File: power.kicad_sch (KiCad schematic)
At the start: 78 parts, among them J3 Vcore_sel, U1 TLV62569DBV, U3 MPM3833CGRH-Z, U4 GateMate-CCGM1A1, U5 TLV62569DBV

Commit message: Initial version of 0.2
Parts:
- R105, R106, R23: value 1R -> 4R7
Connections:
- net VDD_CORE: now also C127.1, C128.1, C42.1; no longer C120.1, C121.1, C122.1, C123.1, C124.1, C125.1, C33.1, C36.1, C39.1
- net VDD_PLL: now also C33.1, C36.1, C39.1; no longer C42.1
- net VDD_SER: now also C121.1, C123.1, C125.1; no longer C128.1
- net VDD_SER_PLL: now also C120.1, C122.1, C124.1; no longer C127.1
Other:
- note removed: "Needs to be 3.3V input"
- moved on the sheet: C120, C121, C122, C123, C124, C125, C127, C128, C2, C33, C36, C39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

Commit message: Update stackup
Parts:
- R105, R106, R23: value 4R7 -> 2R
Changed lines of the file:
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@@
 			)
 		)
-		(property "Value" "4R7"
+		(property "Value" "2R"
 			(at 151.13 114.3 90)
 			(show_name no)
@@
 			)
 		)
-		(property "Value" "4R7"
+		(property "Value" "2R"
 			(at 152.4 88.9 90)
 			(show_name no)
@@
 			)
 		)
-		(property "Value" "4R7"
+		(property "Value" "2R"
 			(at 152.4 140.462 90)
 			(show_name no)

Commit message: M2 key update - changing resistors back to 1R
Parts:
- R105, R106, R23: value 2R -> 1R; LCSC (none) -> C22936
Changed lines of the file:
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@@
 			)
 		)
-		(property "Value" "2R"
+		(property "Value" "1R"
 			(at 151.13 114.3 90)
 			(show_name no)
@@
 			)
 		)
-		(property "LCSC" ""
+		(property "LCSC" "C22936"
 			(at 151.13 111.76 0)
 			(hide yes)
@@
 			)
 		)
-		(property "Value" "2R"
+		(property "Value" "1R"
 			(at 152.4 88.9 90)
 			(show_name no)
@@
 			)
 		)
-		(property "LCSC" ""
+		(property "LCSC" "C22936"
 			(at 152.4 86.36 0)
 			(hide yes)
@@
 			)
 		)
-		(property "Value" "2R"
+		(property "Value" "1R"
 			(at 152.4 140.462 90)
 			(show_name no)
@@
 			)
 		)
-		(property "LCSC" ""
+		(property "LCSC" "C22936"
 			(at 152.4 138.43 0)
 			(hide yes)

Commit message: initial version of ULX5-PCIe-1x
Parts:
- J3: footprint Jumper:SolderJumper-3_P1.3mm_Open_RoundedPad1.0x1.5mm -> Jumper:SolderJumper-3_P1.3mm_Bridged2Bar12_RoundedPad1.0x1.5mm
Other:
- note added: "Not used - for now - colud be used for MIPI?"

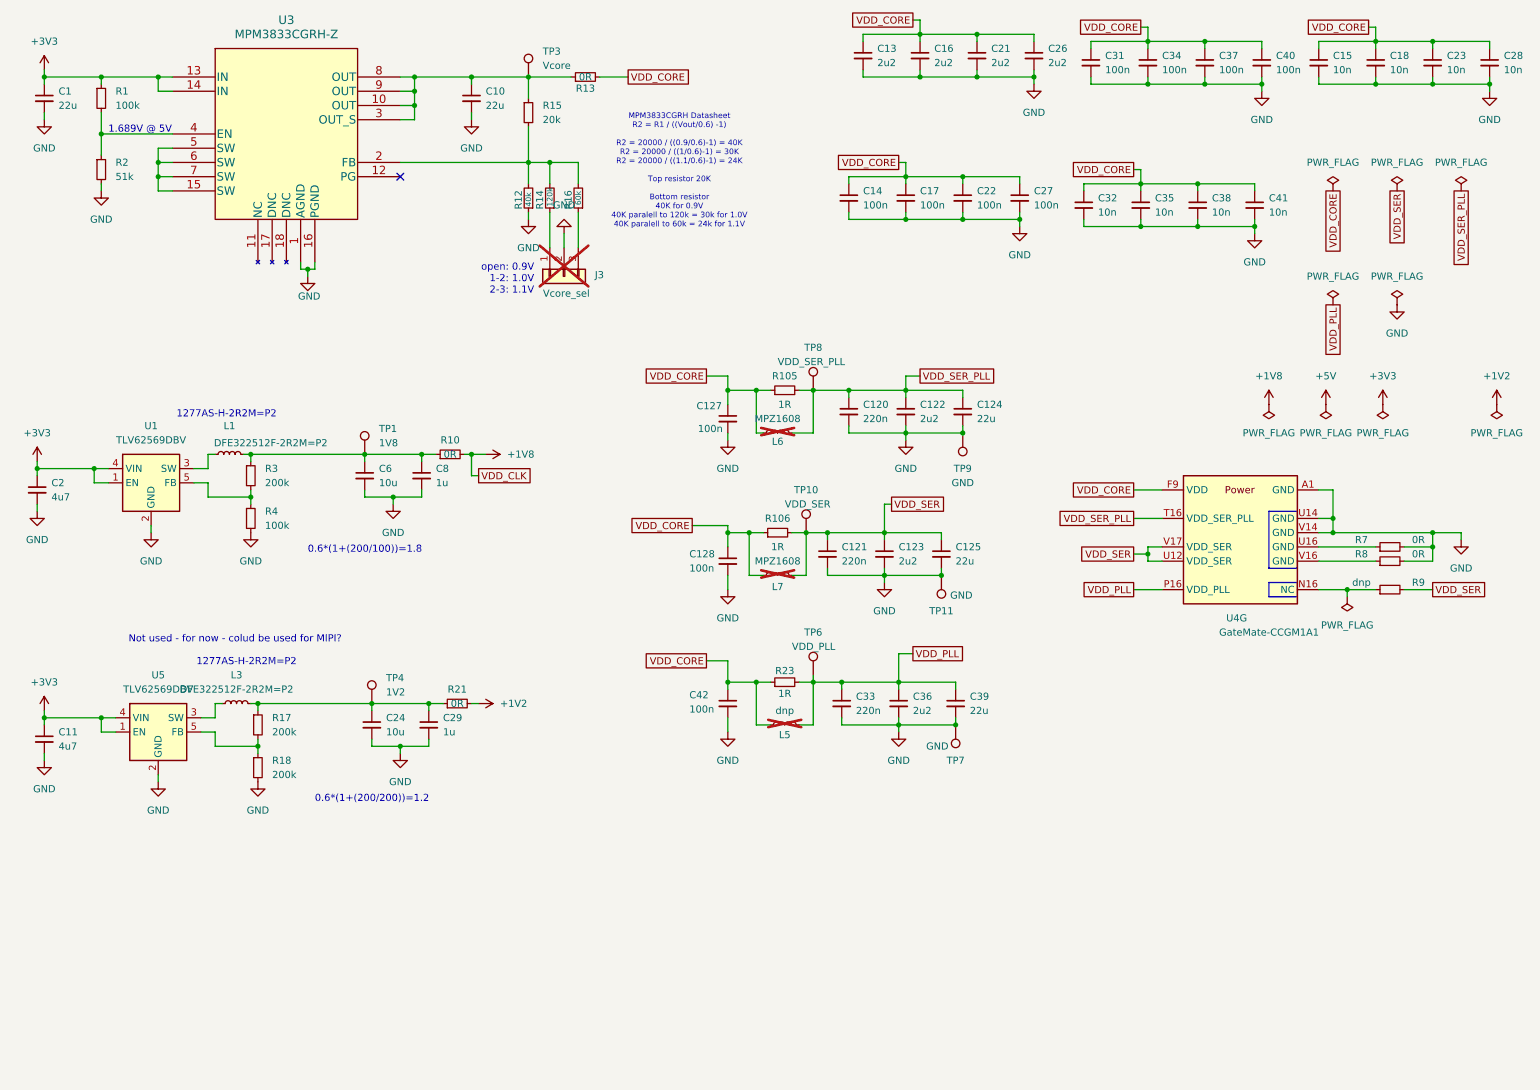
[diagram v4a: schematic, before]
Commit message: Adding 12V PSU
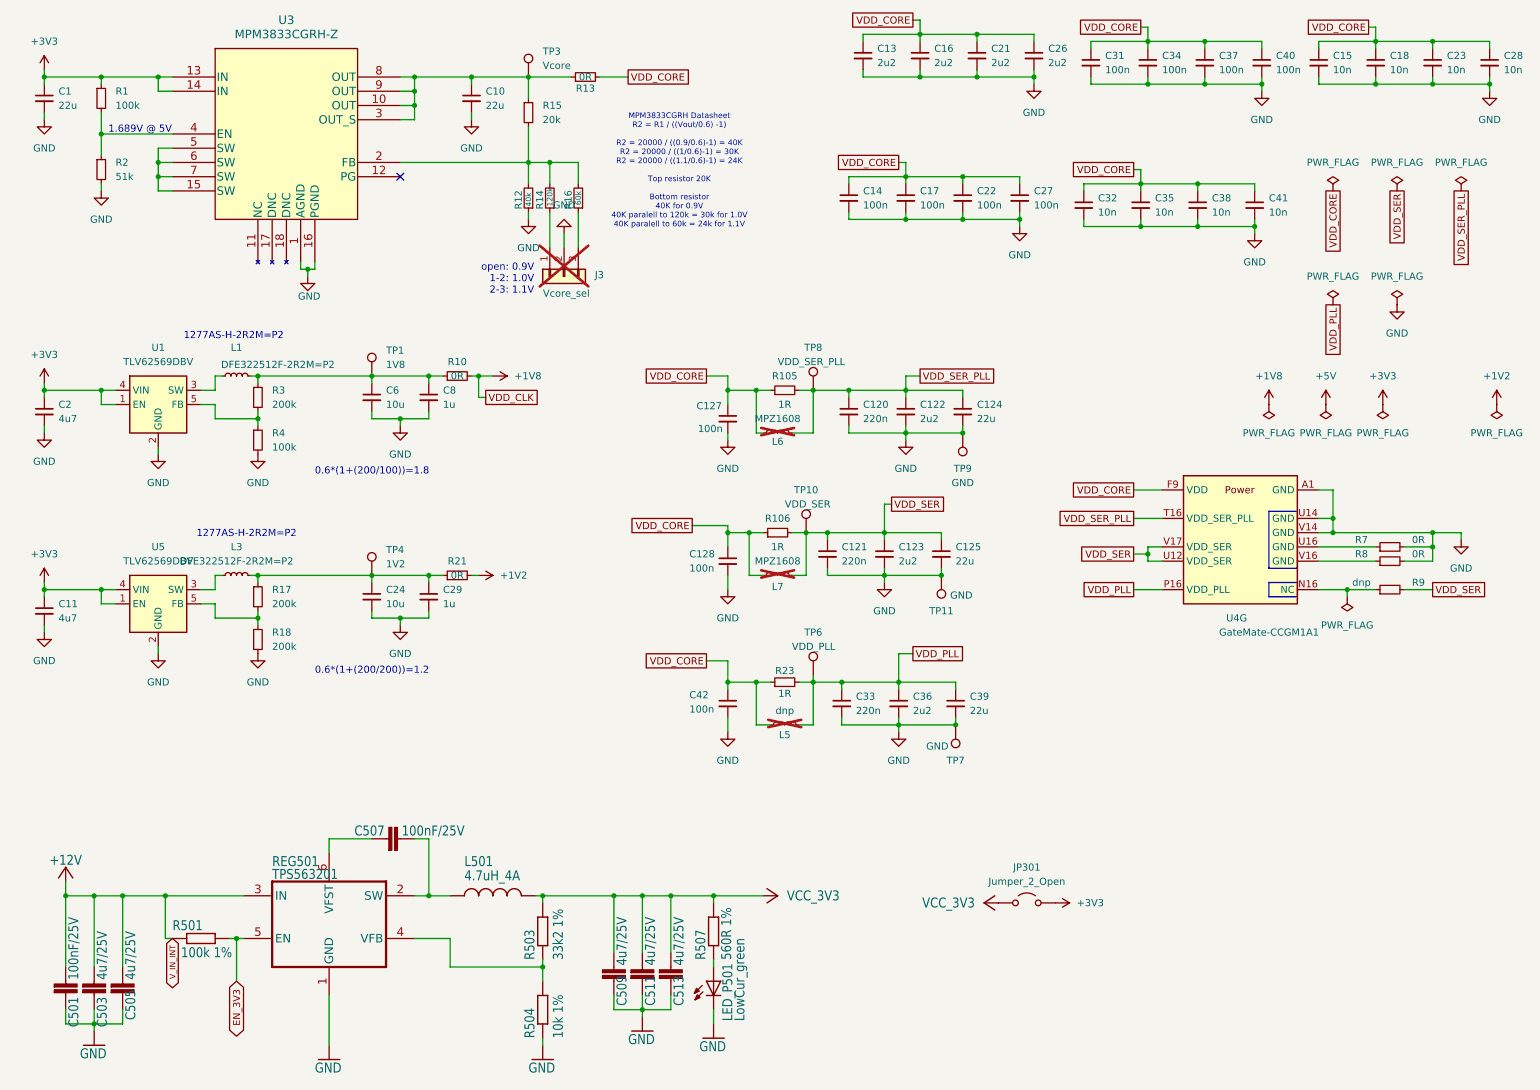
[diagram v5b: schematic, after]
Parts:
- added C501, C507: 100nF/25V, Capacitor_SMD:C_0402_1005Metric, symbol M-SU-12V-v1r1-eagle-import:C0402
- added C503, C505, C509, C511, C513: 4u7/25V, Capacitor_SMD:C_0402_1005Metric, symbol M-SU-12V-v1r1-eagle-import:C0402
- added JP301: Jumper_2_Open, Jumper:SolderJumper-2_P1.3mm_Open_RoundedPad1.0x1.5mm, symbol Jumper:Jumper_2_Open
- added L501: 4.7uH_4A, M-SU-12V-v1r1-import-fps:YSPI0530, symbol M-SU-12V-v1r1-eagle-import:YSPI0530
- added LED_P501: LowCur_green, LED_SMD:LED_0603_1608Metric, symbol M-SU-12V-v1r1-eagle-import:LED0603
- added R501: 100k 1%, Resistor_SMD:R_0402_1005Metric, symbol M-SU-12V-v1r1-eagle-import:R0402
- added R503: 33k2 1%, Resistor_SMD:R_0402_1005Metric, symbol M-SU-12V-v1r1-eagle-import:R0402
- added R504: 10k 1%, Resistor_SMD:R_0402_1005Metric, symbol M-SU-12V-v1r1-eagle-import:R0402
- added R507: 560R 1%, Resistor_SMD:R_0402_1005Metric, symbol M-SU-12V-v1r1-eagle-import:R0402
- added REG501: TPS563201, M-SU-12V-v1r1-import-fps:SOT-23-THIN, symbol M-SU-12V-v1r1-eagle-import:TPS563201
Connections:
- net +3V3: now also JP301.2 (B)
- net GND: now also C501.2, C503.2, C505.2, C509.2, C511.2, C513.2, LED_P501.C, R504.1, REG501.1 (GND)
- new net: C507.1, L501.1, REG501.2 (SW)
- new net: C507.2, REG501.6 (VFST)
- new net: R503.1, R504.2, REG501.4 (VFB)
- new net: LED_P501.A, R507.1
- new net +12V: C501.1, C503.1, C505.1, R501.1, REG501.3 (IN)
- new net EN_3V3: R501.2, REG501.5 (EN)
- new net VCC_3V3: C509.1, C511.1, C513.1, JP301.1 (A), L501.2, R503.2, R507.2
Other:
- note removed: "Not used - for now - colud be used for MIPI?"
- moved on the sheet: C11, C2, C24, C29, C6, C8, L1, L3, R10, R17, R18, R21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

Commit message: Pair switch
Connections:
- net GND: now also LED_P501.1; no longer LED_P501.C
- net at R507.1: now also LED_P501.2; no longer LED_P501.A
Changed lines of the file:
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@@
 			)
 		)
-		(pin "C"
+		(property "LCSC" ""
+			(at 139.7 191.77 0)
+			(hide yes)
+			(show_name no)
+			(do_not_autoplace no)
+			(effects
+				(font
+					(size 1.27 1.27)
+				)
+			)
 		)
-		(pin "A"
+		(pin "2"
+		)
+		(pin "1"
 		)
 		(instances

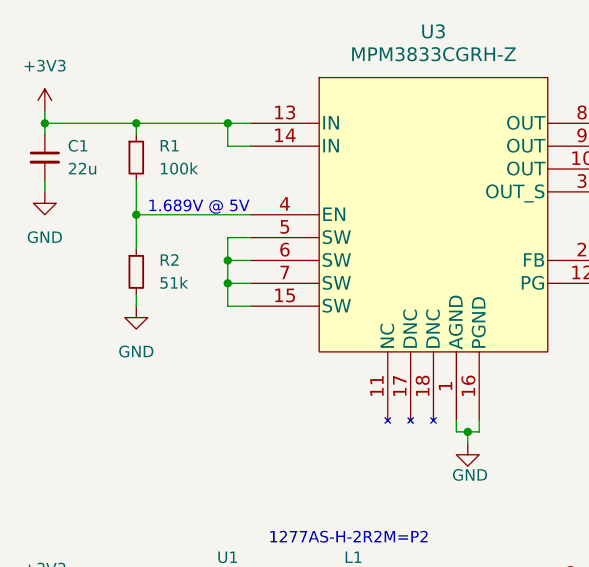
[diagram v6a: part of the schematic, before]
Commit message: power enable fix - connecting AGND
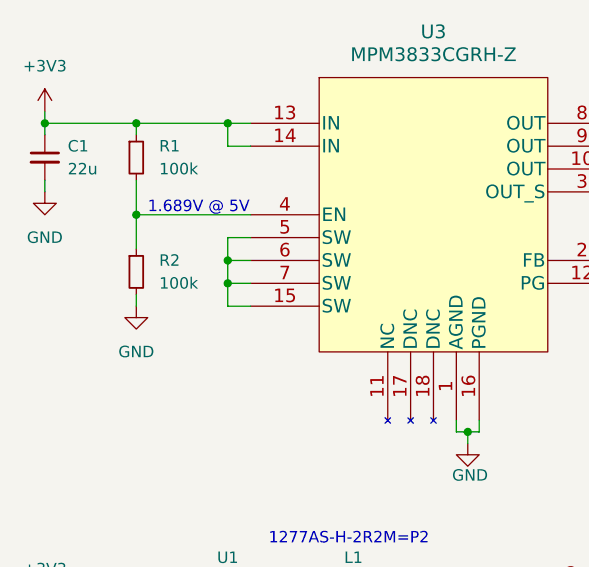
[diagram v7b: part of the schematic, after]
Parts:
- R2: value 51k -> 100k
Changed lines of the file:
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@@
 			)
 		)
-		(property "Value" "51k"
+		(property "Value" "100k"
 			(at 33.02 48.26 0)
 			(show_name no)
@@
 			(at 30.48 46.99 0)
 			(hide yes)
+			(show_name no)
+			(do_not_autoplace no)
+			(effects
+				(font
+					(size 1.27 1.27)
+				)
+			)
+		)
+		(property "LCSC" ""
+			(at 30.48 46.99 0)
+			(hide yes)
